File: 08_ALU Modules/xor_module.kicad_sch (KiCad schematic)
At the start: 3 parts, among them U16 74LS86, U17 74LS86, U18 74LS245

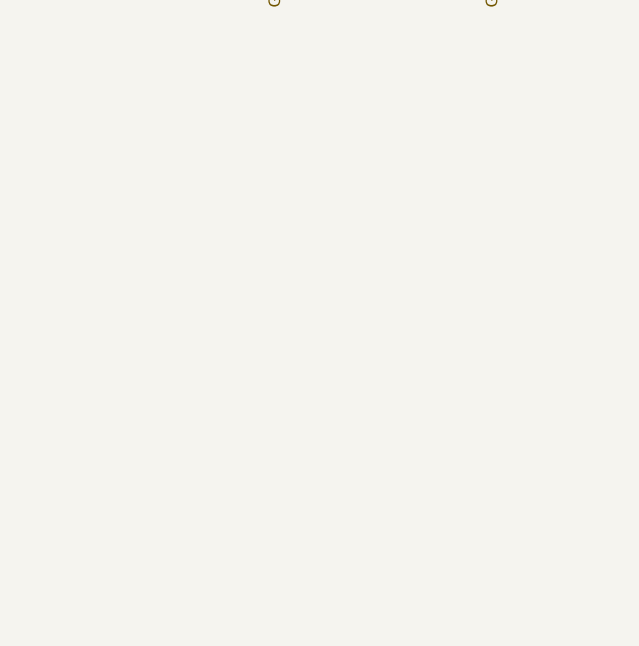
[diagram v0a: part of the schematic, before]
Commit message: Last revision of the cpu, all boards have been ordered. Implementation to be tested and documented in following commits.
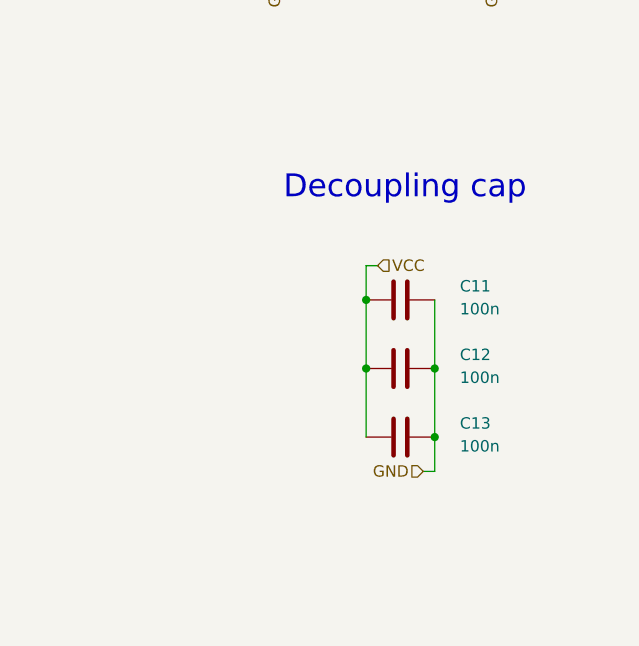
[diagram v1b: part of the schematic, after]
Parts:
- added C11, C12, C13: 100n, Capacitor_THT:C_Disc_D3.0mm_W1.6mm_P2.50mm, symbol Device:C
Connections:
- net GND: now also C11.2, C12.2, C13.2
- net VCC: now also C11.1, C12.1, C13.1
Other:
- note added: "Decoupling cap"
